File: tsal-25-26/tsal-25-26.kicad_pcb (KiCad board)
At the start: 2 copper layers, 87.6 x 36.8 mm, 30 parts, among them J1 043045-0412, Q1 DMP2035U-7, Q3 UJ3N065080K3S, Q4 DMN2056U, Q5 AO3401A, U1 H11L1M, U2 NE555D

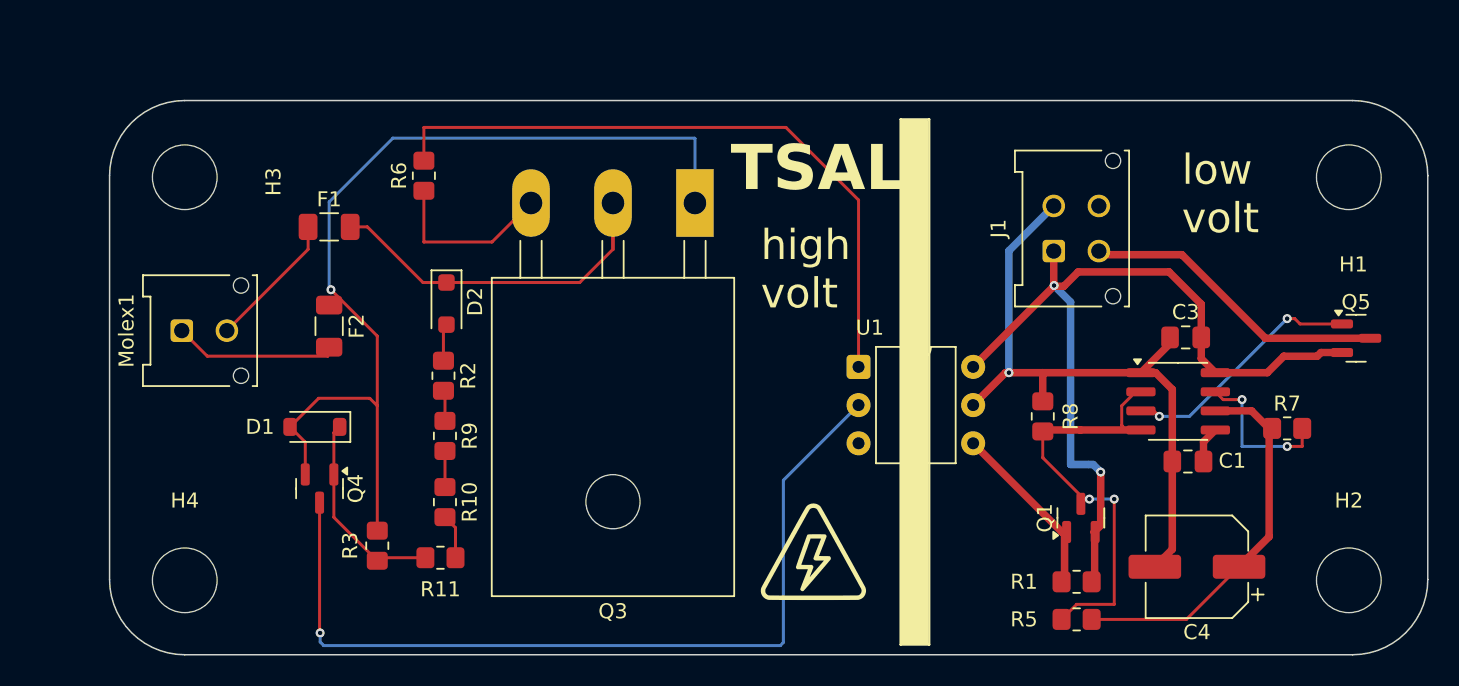
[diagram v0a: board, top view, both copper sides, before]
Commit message: new pcb with correct dimensions
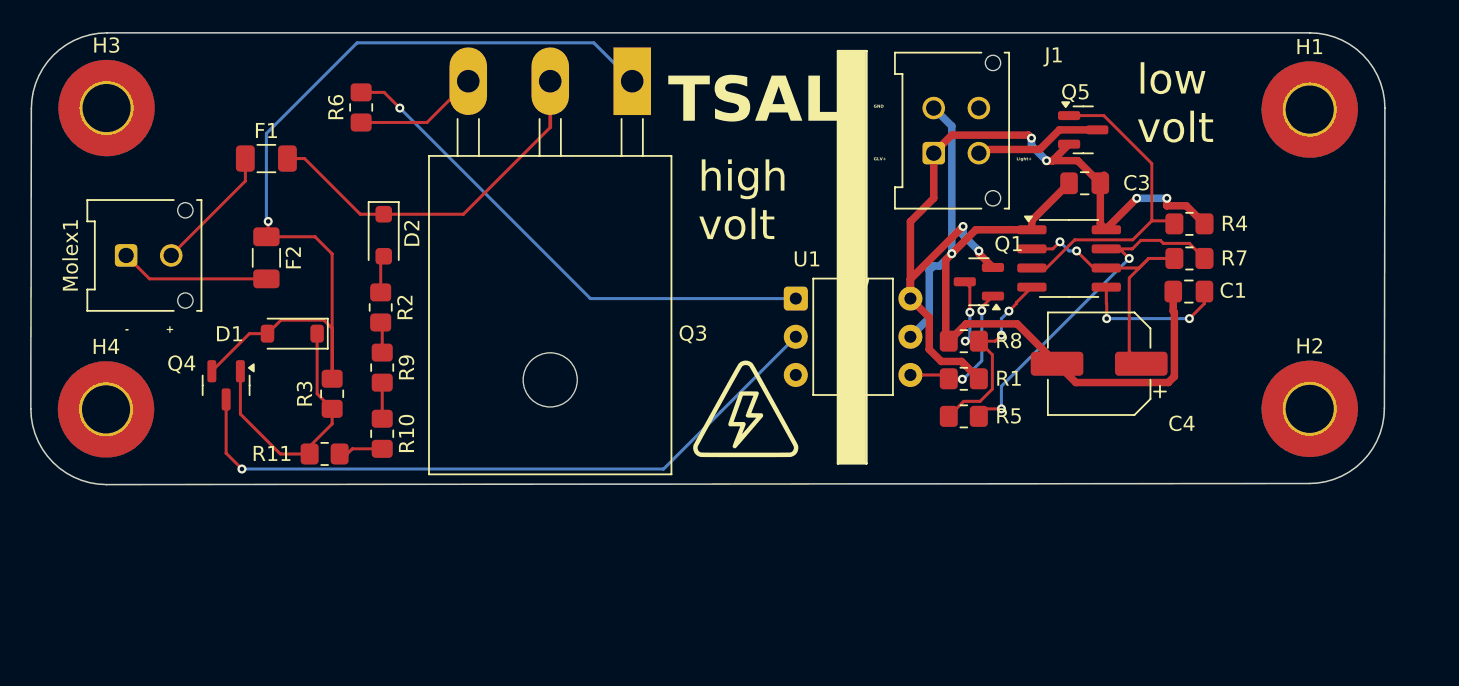
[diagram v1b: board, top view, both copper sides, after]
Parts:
- added R4: 1k, Resistor_SMD:R_0805_2012Metric_Pad1.20x1.40mm_HandSolder, F.Cu at (181.0, 88.2)
- H1, H2, H3, H4: footprint MountingHole:MountingHole_4.3mm_M4 -> MountingHole:MountingHole_3.2mm_M3_Pad_TopBottom
- R5: value 5k -> 100
- moved Q5 22.8 mm to (173.9, 82.0)
- moved Q1 17.1 mm to (167.0, 92.0), turned to 180 degrees
- moved R1 15.4 mm to (166.0, 98.5)
- moved R5 15.4 mm to (166.0, 101.0)
- moved C4 15.0 mm to (175.0, 97.5)
- moved R7 13.0 mm to (181.0, 90.5)
- moved H4 12.5 mm to (109.0, 100.5)
- moved C3 12.3 mm to (174.0, 85.5)
- moved U2 12.0 mm to (173.0, 90.5)
- moved H2 11.7 mm to (189.0, 100.5)
- moved C1 11.3 mm to (181.0, 92.7)
- moved R3 10.5 mm to (124.0, 99.5)
- moved G*** 10.5 mm to (151.5, 100.5)
- moved R11 10.3 mm to (123.5, 103.5)
- moved J1 10.3 mm to (164.0, 83.5)
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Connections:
- R5 pad 2: Net-(U2-THR) -> Net-(U2-DIS)
- U2 pad 2: Net-(Q1-D) -> Net-(U2-THR)
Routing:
- net Net-(U2-DIS): track 10.3 -> 24.3 mm
- net Net-(Q4-D): track 58.1 -> 45.5 mm
- net GND: track 44.2 -> 56.2 mm
- net Net-(Q1-D): track 30.1 -> 18.2 mm, vias 2 -> 4
- net Light+: track 20.4 -> 8.52 mm
- net Net-(R6-Pad2): track 44.2 -> 34.6 mm, vias 0 -> 1
- net Net-(U2-THR): track 26.3 -> 18.5 mm, vias 0 -> 2
- net Net-(U2-CV): track 2.42 -> 9.82 mm, vias 0 -> 2
- net Net-(Q5-G): track 16.4 -> 21.5 mm, vias 2 -> 0
- net Net-(D1-K): track 13.5 -> 17.6 mm
- net Net-(Q3-S): track 11.6 -> 8.26 mm
- net /HV-: track 64.2 -> 61.0 mm
- net Net-(D2-K): track 23.1 -> 24.6 mm
- net Net-(Q1-G): track 11.6 -> 10.4 mm, vias 0 -> 2
- net Net-(Molex1-Pin_1): track 11.1 -> 10.1 mm
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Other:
- board size 87.6 x 36.8 mm -> 90 x 30 mm
- board text added: "+"
- board text added: "-"
- board text added: "GLV+"
- board text added: "GND"
- board text added: "Light+"
